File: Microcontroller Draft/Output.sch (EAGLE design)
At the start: 15 parts

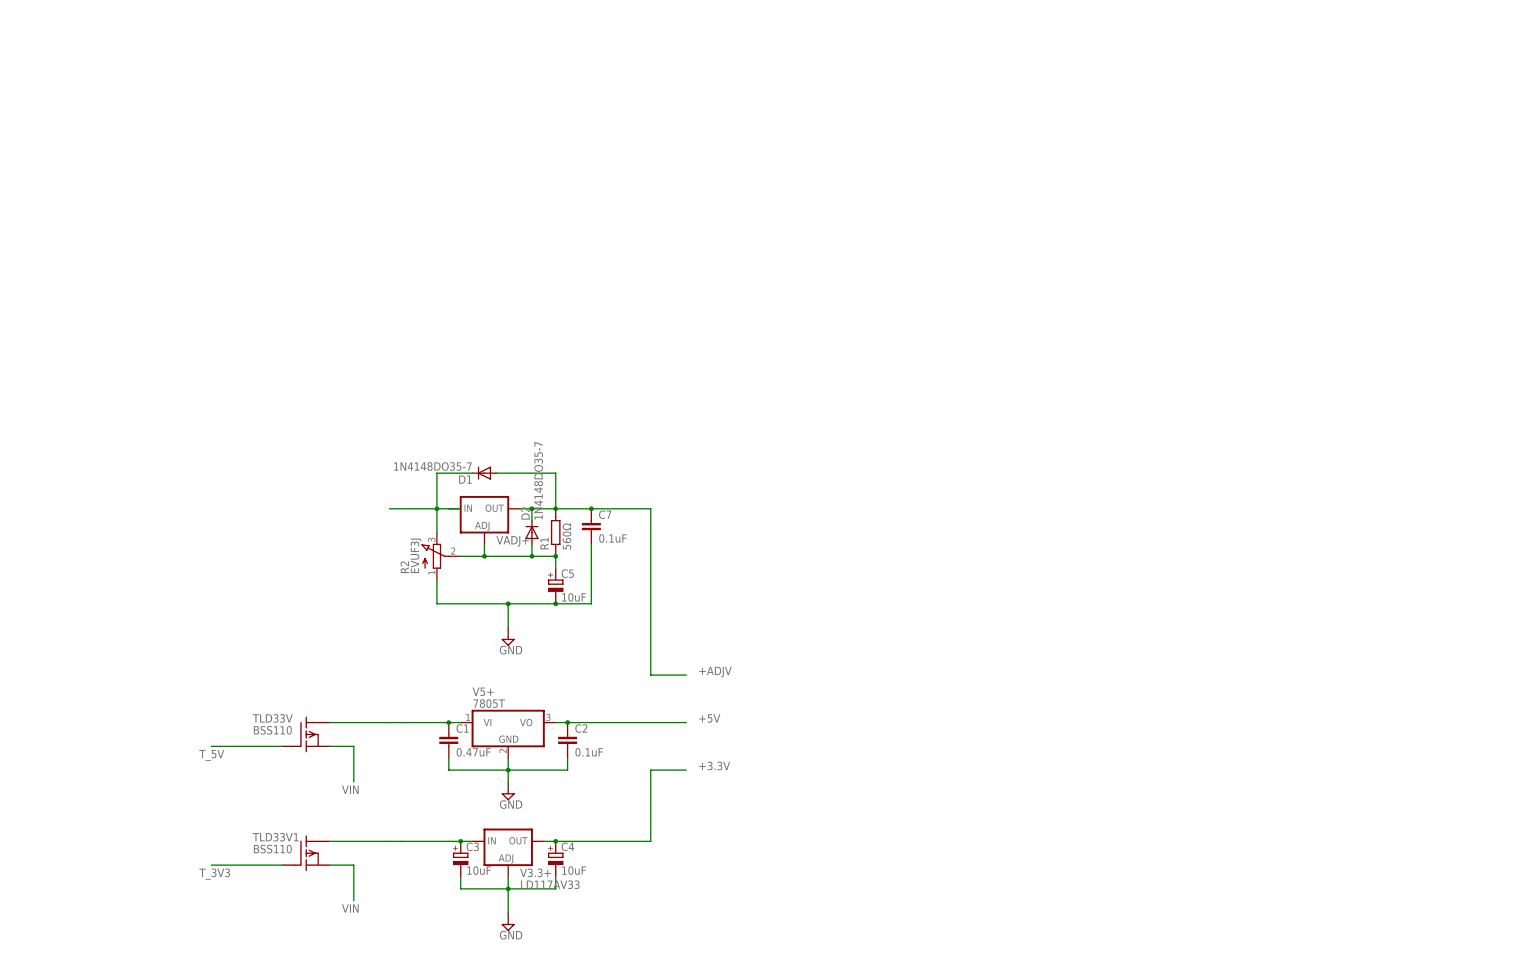
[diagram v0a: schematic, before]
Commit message: Finished the output schematic
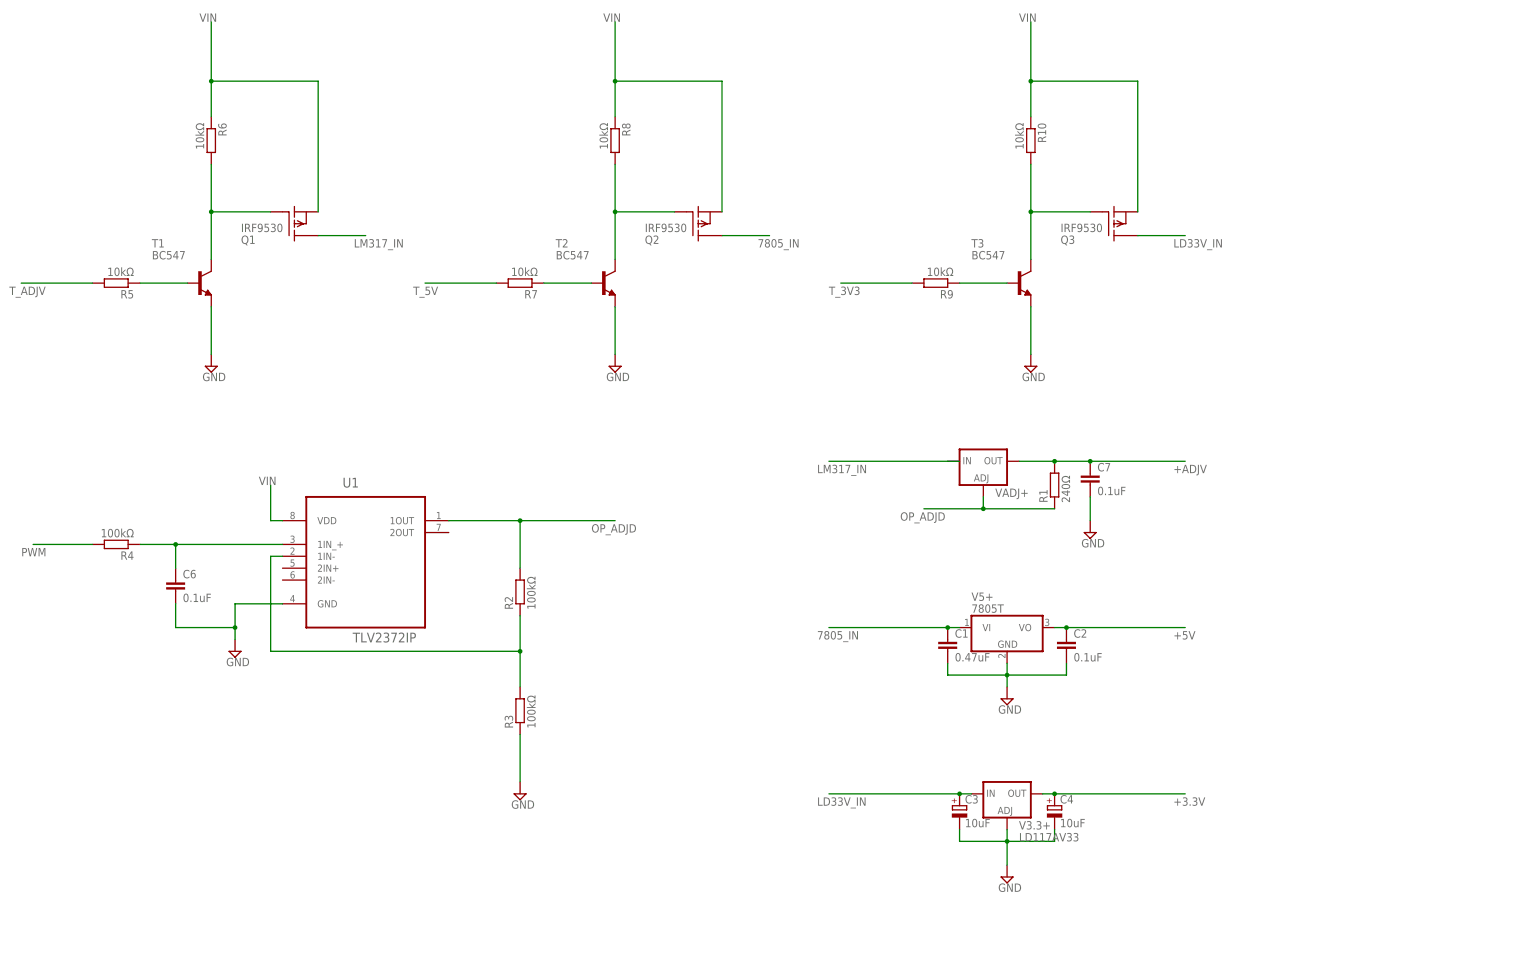
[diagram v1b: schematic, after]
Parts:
- removed C5: 10uF, rcl:CPOL-EUE2.5-6
- removed D1, D2: 1N4148DO35-7, diode:1N4148DO35-7
- removed TLD33V, TLD33V1: BSS110, transistor-fet:BSS110
- added C6: 0.1uF, rcl:C-EU025-025X050
- added Q1, Q2, Q3: IRF9530, transistor-fet:IRF9530
- added R10, R5, R6, R7, R8, R9: 10kΩ, resistor:R-EU_0207/10
- added R3, R4: 100kΩ, resistor:R-EU_0207/10
- added T1, T2, T3: BC547, transistor:BC547
- added U1: TLV2372IP, Texas Instruments_By_element14_Batch_1:TLV2372IP
- R1: value 560Ω -> 240Ω
- R2: value EVUF3J -> 100kΩ; device pot:EVUF3J -> resistor:R-EU_0207/10
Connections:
- removed net N$1: D1.C, R2.E, VADJ+.IN
- removed net N$2: C1.1, TLD33V.D, V5+.VI
- new net 7805_IN: C1.1, Q2.D, V5+.VI
- new net LD33V_IN: C3.+, Q3.D, V3.3+.IN
- new net LM317_IN: Q1.D, VADJ+.IN
- new net N$11: R9.1, T3.B
- new net N$12: Q3.G, R10.2, T3.C
- new net N$3: R2.1, R3.2, U1.1IN-
- new net N$4: R5.1, T1.B
- new net N$5: C6.1, R4.1, U1.1IN_+
- new net N$6: Q1.G, R6.2, T1.C
- new net N$9: Q2.G, R8.2, T2.C
- new net OP_ADJD: R1.1, R2.2, U1.1OUT, VADJ+.ADJ
- new net PWM: R4.2
- new net T_ADJV: R5.2
- net +ADJV: no longer D1.A, D2.C
- net GND: now also C6.2, R3.1, T1.E, T2.E, T3.E, U1.GND; no longer C5.-, R2.A
- net N$8: now also R7.1, T2.B; no longer C5.+, D2.A, R1.1, R2.S, VADJ+.ADJ
- net T_3V3: now also R9.2; no longer TLD33V1.G
- net T_5V: now also R7.2; no longer TLD33V.G
- net VIN: now also Q1.S, Q2.S, Q3.S, R10.1, R6.1, R8.1, U1.VDD; no longer C3.+, TLD33V.S, TLD33V1.D, TLD33V1.S, V3.3+.IN
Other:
- moved on the sheet: C1, C2, C3, C4, C7, R1, V3.3+, V5+, VADJ+

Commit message: Finished the individual schematics
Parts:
- added C5: 0.1uF, rcl:C-EU025-025X050
- added CON_7805, CON_LD33V, CON_LM317: M02JST-PTH-2, SparkFun-Connectors:M02JST-PTH-2
- added JP_7805, JP_LD33V, JP_LM317\: (no value), pinhead:PINHD-1X2
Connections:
- net OP_ADJD renamed LM317_ADJ
- removed net +3.3V: C4.+, V3.3+.OUT
- removed net +5V: C2.1, V5+.VO
- removed net +ADJV: C7.1, R1.2, VADJ+.OUT
- new net 7805_OUT: C2.1, JP_7805.1, V5+.VO
- new net LD33V_OUT: C4.+, JP_LD33V.1, V3.3+.OUT
- new net LM317_OUT: C7.1, JP_LM317\.1, R1.2, VADJ+.OUT
- new net N$13: CON_7805.2, JP_7805.2
- new net N$14: CON_LD33V.2, JP_LD33V.2
- new net N$7: CON_LM317.2, JP_LM317\.2
- net GND: now also C5.2, CON_7805.1, CON_LD33V.1, CON_LM317.1
- net VIN: now also C5.1
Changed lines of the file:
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@@
 <layer number="51" name="tDocu" color="6" fill="1" visible="no" active="no"/>
 <layer number="52" name="bDocu" color="7" fill="1" visible="no" active="no"/>
+<layer number="53" name="tGND_GNDA" color="7" fill="9" visible="no" active="no"/>
+<layer number="54" name="bGND_GNDA" color="1" fill="9" visible="no" active="no"/>
+<layer number="56" name="wert" color="7" fill="1" visible="no" active="no"/>
 <layer number="91" name="Nets" color="2" fill="1" visible="yes" active="yes"/>
 <layer number="92" name="Busses" color="1" fill="1" visible="yes" active="yes"/>
@@
 <layer number="123" name="tTestmark" color="7" fill="1" visible="yes" active="yes"/>
 <layer number="124" name="bTestmark" color="7" fill="1" visible="yes" active="yes"/>
+<layer number="125" name="_tNames" color="7" fill="1" visible="yes" active="yes"/>
 <layer number="131" name="tAdjust" color="7" fill="1" visible="yes" active="yes"/>
 <layer number="132" name="bAdjust" color="7" fill="1" visible="yes" active="yes"/>
+<layer number="144" name="Drill_legend" color="7" fill="1" visible="yes" active="yes"/>
+<layer number="151" name="HeatSink" color="7" fill="1" visible="yes" active="yes"/>
+<layer number="199" name="Contour" color="7" fill="1" visible="yes" active="yes"/>
 <layer number="200" name="200bmp" color="7" fill="1" visible="yes" active="yes"/>
 <layer number="201" name="201bmp" color="7" fill="1" visible="yes" active="yes"/>
@@
 <layer number="209" name="209bmp" color="7" fill="1" visible="yes" active="yes"/>
 <layer number="210" name="210bmp" color="7" fill="1" visible="yes" active="yes"/>
+<layer number="211" name="211bmp" color="7" fill="1" visible="yes" active="yes"/>
+<layer number="212" name="212bmp" color="7" fill="1" visible="yes" active="yes"/>
+<layer number="213" name="213bmp" color="7" fill="1" visible="yes" active="yes"/>
+<layer number="214" name="214bmp" color="7" fill="1" visible="yes" active="yes"/>
+<layer number="215" name="215bmp" color="7" fill="1" visible="yes" active="yes"/>
+<layer number="216" name="216bmp" color="7" fill="1" visible="yes" active="yes"/>
+<layer number="217" name="217bmp" color="18" fill="1" visible="no" active="no"/>
+<layer number="218" name="218bmp" color="19" fill="1" visible="no" active="no"/>
+<layer number="219" name="219bmp" color="20" fill="1" visible="no" active="no"/>
+<layer number="220" name="220bmp" color="21" fill="1" visible="no" active="no"/>
+<layer number="221" name="221bmp" color="22" fill="1" visible="no" active="no"/>
+<layer number="222" name="222bmp" color="23" fill="1" visible="no" active="no"/>
+<layer number="223" name="223bmp" color="24" fill="1" visible="no" active="no"/>
+<layer number="224" name="224bmp" color="25" fill="1" visible="no" active="no"/>
 <layer number="250" name="Descript" color="3" fill="1" visible="no" active="no"/>
 <layer number="251" name="SMDround" color="12" fill="11" visible="no" active="no"/>
@@
 <part name="R10" library="resistor" deviceset="R-EU_" device="0207/10" value="10kΩ"/>
 <part name="SUPPLY8" library="supply2" deviceset="GND" device=""/>
+<part name="SUPPLY9" library="supply2" deviceset="GND" device=""/>
+<part name="C5" library="rcl" deviceset="C-EU" device="025-025X050" value="0.1uF"/>
+<part name="JP_LM317\" library="pinhead" deviceset="PINHD-1X2" device=""/>
+<part name="JP_7805" library="pinhead" deviceset="PINHD-1X2" device=""/>
+<part name="JP_LD33V" library="pinhead" deviceset="PINHD-1X2" device=""/>
+<part name="CON_LM317" library="SparkFun-Connectors" deviceset="M02" device="JST-PTH-2"/>
+<part name="CON_7805" library="SparkFun-Connectors" deviceset="M02" device="JST-PTH-2"/>
+<part name="CON_LD33V" library="SparkFun-Connectors" deviceset="M02" device="JST-PTH-2"/>
+<part name="SUPPLY10" library="supply2" deviceset="GND" device=""/>
+<part name="SUPPLY11" library="supply2" deviceset="GND" device=""/>
+<part name="SUPPLY12" library="supply2" deviceset="GND" device=""/>
 </parts>
 <sheets>
@@
 <instance part="R10" gate="G$1" x="223.52" y="167.64" rot="R270"/>
 <instance part="SUPPLY8" gate="GND" x="223.52" y="119.38"/>
+<instance part="SUPPLY9" gate="GND" x="45.72" y="88.9"/>
+<instance part="C5" gate="G$1" x="45.72" y="99.06"/>
+<instance part="JP_LM317\" gate="G$1" x="307.34" y="111.76" rot="R90"/>
+<instance part="JP_7805" gate="G$1" x="307.34" y="76.2" rot="R90"/>
+<instance part="JP_LD33V" gate="G$1" x="307.34" y="40.64" rot="R90"/>
+<instance part="CON_LM317" gate="G$1" x="327.66" y="101.6" rot="R180"/>
+<instance part="CON_7805" gate="G$1" x="327.66" y="66.04" rot="R180"/>
+<instance part="CON_LD33V" gate="G$1" x="327.66" y="30.48" rot="R180"/>
+<instance part="SUPPLY10" gate="GND" x="317.5" y="88.9"/>
+<instance part="SUPPLY11" gate="GND" x="317.5" y="53.34"/>
+<instance part="SUPPLY12" gate="GND" x="317.5" y="17.78"/>
 </instances>
 <busses>
 </busses>
 <nets>
-<net name="+3.3V" class="0">
+<net name="LD33V_OUT" class="0">
 <segment>
 <pinref part="V3.3+" gate="G$1" pin="OUT"/>
@@
 <label x="254" y="25.4" size="1.778" layer="95"/>
 </segment>
+<segment>
+<pinref part="JP_LD33V" gate="G$1" pin="1"/>
+<wire x1="304.8" y1="38.1" x2="304.8" y2="27.94" width="0.1524" layer="91"/>
+<wire x1="304.8" y1="27.94" x2="292.1" y2="27.94" width="0.1524" layer="91"/>
+<label x="281.94" y="25.4" size="1.778" layer="95"/>
+</segment>
 </net>
 <net name="VIN" class="0">
@@
 <pinref part="U1" gate="A" pin="VDD"/>
 <wire x1="63.5" y1="86.36" x2="60.96" y2="86.36" width="0.1524" layer="91"/>
-<wire x1="60.96" y1="86.36" x2="60.96" y2="93.98" width="0.1524" layer="91"/>
-<label x="58.42" y="93.98" size="1.778" layer="95"/>
+<wire x1="60.96" y1="86.36" x2="60.96" y2="91.44" width="0.1524" layer="91"/>
+<label x="58.42" y="99.06" size="1.778" layer="95"/>
+<pinref part="C5" gate="G$1" pin="1"/>
+<wire x1="60.96" y1="91.44" x2="60.96" y2="99.06" width="0.1524" layer="91"/>
+<wire x1="45.72" y1="101.6" x2="45.72" y2="104.14" width="0.1524" layer="91"/>
+<wire x1="45.72" y1="104.14" x2="55.88" y2="104.14" width="0.1524" layer="91"/>
+<wire x1="55.88" y1="104.14" x2="55.88" y2="91.44" width="0.1524" layer="91"/>
+<wire x1="55.88" y1="91.44" x2="60.96" y2="91.44" width="0.1524" layer="91"/>
+<junction x="60.96" y="91.44"/>
 </segment>
 <segment>
@@
 </segment>
 </net>
-<net name="+5V" class="0">
+<net name="7805_OUT" class="0">
 <segment>
 <pinref part="V5+" gate="A1" pin="VO"/>
@@
 <wire x1="231.14" y1="63.5" x2="256.54" y2="63.5" width="0.1524" layer="91"/>
 <label x="254" y="60.96" size="1.778" layer="95"/>
+</segment>
+<segment>
+<pinref part="JP_7805" gate="G$1" pin="1"/>
+<wire x1="304.8" y1="73.66" x2="304.8" y2="63.5" width="0.1524" layer="91"/>
+<wire x1="304.8" y1="63.5" x2="292.1" y2="63.5" width="0.1524" layer="91"/>
+<label x="284.48" y="60.96" size="1.778" layer="95"/>
 </segment>
 </net>
@@
 <wire x1="223.52" y1="132.08" x2="223.52" y2="121.92" width="0.1524" layer="91"/>
 </segment>
-</net>
-<net name="+ADJV" class="0">
+<segment>
+<pinref part="SUPPLY9" gate="GND" pin="GND"/>
+<pinref part="C5" gate="G$1" pin="2"/>
+<wire x1="45.72" y1="91.44" x2="45.72" y2="93.98" width="0.1524" layer="91"/>
+</segment>
+<segment>
+<pinref part="CON_LM317" gate="G$1" pin="1"/>
+<wire x1="320.04" y1="101.6" x2="317.5" y2="101.6" width="0.1524" layer="91"/>
+<wire x1="317.5" y1="101.6" x2="317.5" y2="91.44" width="0.1524" layer="91"/>
+<pinref part="SUPPLY10" gate="GND" pin="GND"/>
+</segment>
+<segment>
+<pinref part="CON_7805" gate="G$1" pin="1"/>
+<wire x1="320.04" y1="66.04" x2="317.5" y2="66.04" width="0.1524" layer="91"/>
+<wire x1="317.5" y1="66.04" x2="317.5" y2="55.88" width="0.1524" layer="91"/>
+<pinref part="SUPPLY11" gate="GND" pin="GND"/>
+</segment>
+<segment>
+<pinref part="CON_LD33V" gate="G$1" pin="1"/>
+<wire x1="320.04" y1="30.48" x2="317.5" y2="30.48" width="0.1524" layer="91"/>
+<wire x1="317.5" y1="30.48" x2="317.5" y2="20.32" width="0.1524" layer="91"/>
+<pinref part="SUPPLY12" gate="GND" pin="GND"/>
+</segment>
+</net>
+<net name="LM317_OUT" class="0">
 <segment>
 <pinref part="VADJ+" gate="A" pin="OUT"/>
@@
 <label x="254" y="96.52" size="1.778" layer="95"/>
 </segment>
+<segment>
+<pinref part="JP_LM317\" gate="G$1" pin="1"/>
+<wire x1="304.8" y1="109.22" x2="304.8" y2="99.06" width="0.1524" layer="91"/>
+<wire x1="304.8" y1="99.06" x2="292.1" y2="99.06" width="0.1524" layer="91"/>
+<label x="281.94" y="96.52" size="1.778" layer="95"/>
+</segment>
 </net>
 <net name="LM317_IN" class="0">
@@
 </segment>
 </net>
-<net name="OP_ADJD" class="0">
+<net name="LM317_ADJ" class="0">
 <segment>
 <pinref part="R2" gate="G$1" pin="2"/>
@@
 </segment>
 </net>
+<net name="N$7" class="0">
+<segment>
+<pinref part="JP_LM317\" gate="G$1" pin="2"/>
+<wire x1="307.34" y1="109.22" x2="307.34" y2="99.06" width="0.1524" layer="91"/>
+<wire x1="307.34" y1="99.06" x2="320.04" y2="99.06" width="0.1524" layer="91"/>
+<pinref part="CON_LM317" gate="G$1" pin="2"/>
+</segment>
+</net>
+<net name="N$13" class="0">
+<segment>
+<pinref part="JP_7805" gate="G$1" pin="2"/>
+<wire x1="307.34" y1="73.66" x2="307.34" y2="63.5" width="0.1524" layer="91"/>
+<wire x1="307.34" y1="63.5" x2="320.04" y2="63.5" width="0.1524" layer="91"/>
+<pinref part="CON_7805" gate="G$1" pin="2"/>
+</segment>
+</net>
+<net name="N$14" class="0">
+<segment>
+<pinref part="JP_LD33V" gate="G$1" pin="2"/>
+<wire x1="307.34" y1="38.1" x2="307.34" y2="27.94" width="0.1524" layer="91"/>
+<wire x1="307.34" y1="27.94" x2="320.04" y2="27.94" width="0.1524" layer="91"/>
+<pinref part="CON_LD33V" gate="G$1" pin="2"/>
+</segment>
+</net>

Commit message: Fixed some errors
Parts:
- renumbered JP_LM317\ to JP_LM317
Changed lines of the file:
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@@
 <part name="SUPPLY9" library="supply2" deviceset="GND" device=""/>
 <part name="C5" library="rcl" deviceset="C-EU" device="025-025X050" value="0.1uF"/>
-<part name="JP_LM317\" library="pinhead" deviceset="PINHD-1X2" device=""/>
+<part name="JP_LM317" library="pinhead" deviceset="PINHD-1X2" device=""/>
 <part name="JP_7805" library="pinhead" deviceset="PINHD-1X2" device=""/>
 <part name="JP_LD33V" library="pinhead" deviceset="PINHD-1X2" device=""/>
@@
 <instance part="SUPPLY9" gate="GND" x="45.72" y="88.9"/>
 <instance part="C5" gate="G$1" x="45.72" y="99.06"/>
-<instance part="JP_LM317\" gate="G$1" x="307.34" y="111.76" rot="R90"/>
+<instance part="JP_LM317" gate="G$1" x="307.34" y="111.76" rot="R90"/>
 <instance part="JP_7805" gate="G$1" x="307.34" y="76.2" rot="R90"/>
 <instance part="JP_LD33V" gate="G$1" x="307.34" y="40.64" rot="R90"/>
@@
 </segment>
 <segment>
-<pinref part="JP_LM317\" gate="G$1" pin="1"/>
+<pinref part="JP_LM317" gate="G$1" pin="1"/>
 <wire x1="304.8" y1="109.22" x2="304.8" y2="99.06" width="0.1524" layer="91"/>
 <wire x1="304.8" y1="99.06" x2="292.1" y2="99.06" width="0.1524" layer="91"/>
@@
 <net name="LM317_IN" class="0">
 <segment>
-<wire x1="205.74" y1="99.06" x2="208.28" y2="99.06" width="0.1524" layer="91"/>
 <pinref part="VADJ+" gate="A" pin="IN"/>
 <wire x1="205.74" y1="99.06" x2="180.34" y2="99.06" width="0.1524" layer="91"/>
@@
 <net name="N$7" class="0">
 <segment>
-<pinref part="JP_LM317\" gate="G$1" pin="2"/>
+<pinref part="JP_LM317" gate="G$1" pin="2"/>
 <wire x1="307.34" y1="109.22" x2="307.34" y2="99.06" width="0.1524" layer="91"/>
 <wire x1="307.34" y1="99.06" x2="320.04" y2="99.06" width="0.1524" layer="91"/>
